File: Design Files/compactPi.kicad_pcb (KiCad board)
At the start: 6 copper layers, 47 x 105 mm, 130 parts, among them J1 1053101208, J10 Conn_01x06_MountingPin, J11 Conn_01x04_MountingPin, J12 Conn_01x02_MountingPin, J13 Conn_01x02_MountingPin, J14 Micro_SD_Card_Det, J15 USB_C_Receptacle_USB2.0, J16 Conn_01x06_MountingPin, J17 Conn_01x06_MountingPin, J18 Conn_01x06_MountingPin, J19 Conn_01x06_MountingPin, J2 HDMI_A_1.4, J3 Conn_01x04_MountingPin, J4 Conn_01x06_MountingPin, J5 Conn_01x04_MountingPin, J6 Conn_01x04_MountingPin, J7 Conn_01x04_MountingPin, J8 Conn_01x04_MountingPin, J9 Conn_01x04_MountingPin, U1 RT9742GGJ5, U13 TLVM13630RDHR, U14 TLVM13630RDHR, U15 AK09918C, U17 RT9742SNGV, U18 PCA9685PW, U19 ICM-20602, U2 AT24CS64-MAHM, U20 MMC5983MA, U21 MCP25625x-x-ML, U22 WE-TVS-82400102, U23 WE-TVS-82400102, U25 BMP390, U4 LM74700QDBVRQ1, U5 CSD18511Q5A, U6 CSD18511Q5A, U7 LM74700QDBVRQ1, U8 CSD18511Q5A, U9 LM74700QDBVRQ1, Y1 Crystal_GND24_Small

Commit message: Added additional ground vias to ethernet nets
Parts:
- moved G*** 4.64 mm to (144.9, 65.3), turned to -90 degrees
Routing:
- net GND: vias 33 -> 41
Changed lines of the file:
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@@
 	(footprint "LOGO"
 		(layer "B.Cu")
-		(at 140.3 64.7 90)
+		(at 144.9 65.3 -90)
 		(property "Reference" "G***"
 			(at 0 0 90)
@@
 				(xy 0.74915 -1.619005) (xy 0.748603 -1.596191) (xy 0.748328 -1.568735) (xy 0.748269 -1.53599) (xy 0.748372 -1.497308)
 				(xy 0.748548 -1.458993) (xy 0.749473 -1.274104) (xy 0.801897 -1.273118) (xy 0.854321 -1.272131)
+			)
+			(stroke
+				(width 0)
+				(type solid)
+			)
+			(fill yes)
+			(layer "B.SilkS")
+		)
+		(fp_poly
+			(pts
+				(xy -0.695313 -1.272295) (xy -0.662953 -1.282153) (xy -0.633599 -1.297835) (xy -0.607944 -1.318779)
+				(xy -0.58668 -1.344421) (xy -0.570498 -1.374199) (xy -0.560211 -1.406976) (xy -0.558999 -1.414101)
+				(xy -0.557981 -1.423469) (xy -0.557141 -1.435672) (xy -0.556466 -1.451302) (xy -0.555941 -1.470949)
+				(xy -0.55555 -1.495207) (xy -0.555279 -1.524666) (xy -0.555112 -1.559919) (xy -0.555036 -1.601556)
+				(xy -0.555029 -1.614044) (xy -0.554967 -1.796951) (xy -0.608501 -1.796951) (xy -0.662035 -1.796951)
+				(xy -0.662106 -1.644379) (xy -0.662204 -1.611007) (xy -0.662456 -1.578981) (xy -0.662843 -1.5492)
+				(xy -0.663347 -1.522559) (xy -0.663949 -1.499954) (xy -0.664632 -1.482283) (xy -0.665376 -1.470441)
+				(xy -0.665733 -1.467201) (xy -0.672772 -1.438931) (xy -0.684784 -1.415502) (xy -0.701378 -1.397241)
+				(xy -0.722161 -1.384474) (xy -0.74674 -1.377526) (xy -0.774685 -1.376721) (xy -0.800997 -1.382033)
+				(xy -0.823447 -1.393306) (xy -0.841754 -1.410327) (xy -0.855637 -1.432884) (xy -0.858828 -1.440518)
+				(xy -0.860373 -1.445006) (xy -0.861658 -1.450061) (xy -0.862708 -1.456344) (xy -0.863547 -1.464516)
+				(xy -0.864198 -1.47524) (xy -0.864683 -1.489175) (xy -0.865028 -1.506984) (xy -0.865255 -1.529327)
+				(xy -0.865387 -1.556866) (xy -0.865449 -1.590262) (xy -0.865463 -1.627465) (xy -0.865463 -1.796951)
+				(xy -0.920805 -1.796951) (xy -0.976146 -1.796951) (xy -0.975231 -1.535527) (xy -0.974315 -1.274104)
+				(xy -0.920782 -1.274104) (xy -0.867248 -1.274104) (xy -0.8662 -1.299961) (xy -0.865151 -1.325818)
+				(xy -0.850735 -1.311966) (xy -0.825406 -1.292467) (xy -0.796048 -1.278801) (xy -0.762603 -1.270947)
+				(xy -0.729987 -1.268826)
 			)
 			(stroke
@@
 				(xy -0.833788 -2.13504) (xy -0.807966 -2.115448) (xy -0.780185 -2.101943) (xy -0.749383 -2.094141)
 				(xy -0.7145 -2.091658)
-			)
-			(stroke
-				(width 0)
-				(type solid)
-			)
-			(fill yes)
-			(layer "B.SilkS")
-		)
-		(fp_poly
-			(pts
-				(xy -0.695313 -1.272295) (xy -0.662953 -1.282153) (xy -0.633599 -1.297835) (xy -0.607944 -1.318779)
-				(xy -0.58668 -1.344421) (xy -0.570498 -1.374199) (xy -0.560211 -1.406976) (xy -0.558999 -1.414101)
-				(xy -0.557981 -1.423469) (xy -0.557141 -1.435672) (xy -0.556466 -1.451302) (xy -0.555941 -1.470949)
-				(xy -0.55555 -1.495207) (xy -0.555279 -1.524666) (xy -0.555112 -1.559919) (xy -0.555036 -1.601556)
-				(xy -0.555029 -1.614044) (xy -0.554967 -1.796951) (xy -0.608501 -1.796951) (xy -0.662035 -1.796951)
-				(xy -0.662106 -1.644379) (xy -0.662204 -1.611007) (xy -0.662456 -1.578981) (xy -0.662843 -1.5492)
-				(xy -0.663347 -1.522559) (xy -0.663949 -1.499954) (xy -0.664632 -1.482283) (xy -0.665376 -1.470441)
-				(xy -0.665733 -1.467201) (xy -0.672772 -1.438931) (xy -0.684784 -1.415502) (xy -0.701378 -1.397241)
-				(xy -0.722161 -1.384474) (xy -0.74674 -1.377526) (xy -0.774685 -1.376721) (xy -0.800997 -1.382033)
-				(xy -0.823447 -1.393306) (xy -0.841754 -1.410327) (xy -0.855637 -1.432884) (xy -0.858828 -1.440518)
-				(xy -0.860373 -1.445006) (xy -0.861658 -1.450061) (xy -0.862708 -1.456344) (xy -0.863547 -1.464516)
-				(xy -0.864198 -1.47524) (xy -0.864683 -1.489175) (xy -0.865028 -1.506984) (xy -0.865255 -1.529327)
-				(xy -0.865387 -1.556866) (xy -0.865449 -1.590262) (xy -0.865463 -1.627465) (xy -0.865463 -1.796951)
-				(xy -0.920805 -1.796951) (xy -0.976146 -1.796951) (xy -0.975231 -1.535527) (xy -0.974315 -1.274104)
-				(xy -0.920782 -1.274104) (xy -0.867248 -1.274104) (xy -0.8662 -1.299961) (xy -0.865151 -1.325818)
-				(xy -0.850735 -1.311966) (xy -0.825406 -1.292467) (xy -0.796048 -1.278801) (xy -0.762603 -1.270947)
-				(xy -0.729987 -1.268826)
 			)
 			(stroke
@@
 	)
 	(gr_text "Copyright © 2026 Logan Fagg, Licensed under CERN-OHL-S v2"
-		(at 146.5 119.3 270)
+		(at 147.3 69.3 90)
 		(layer "B.SilkS")
 		(effects
@@
 	)
 	(via
+		(at 136.9 127.7)
+		(size 0.45)
+		(drill 0.2)
+		(layers "F.Cu" "B.Cu")
+		(free yes)
+		(net 1)
+	)
+	(via
 		(at 142 89.7)
 		(size 0.5)
@@
 	)
 	(via
+		(at 130.3 115.1)
+		(size 0.45)
+		(drill 0.2)
+		(layers "F.Cu" "B.Cu")
+		(free yes)
+		(net 1)
+	)
+	(via
 		(at 108 95.7)
 		(size 0.5)
@@
 	)
 	(via
+		(at 138.1 129.9)
+		(size 0.45)
+		(drill 0.2)
+		(layers "F.Cu" "B.Cu")
+		(free yes)
+		(net 1)
+	)
+	(via
+		(at 140.9 131.3)
+		(size 0.45)
+		(drill 0.2)
+		(layers "F.Cu" "B.Cu")
+		(free yes)
+		(net 1)
+	)
+	(via
 		(at 142 85.2)
 		(size 0.5)
@@
 	)
 	(via
+		(at 127.9 115.1)
+		(size 0.45)
+		(drill 0.2)
+		(layers "F.Cu" "B.Cu")
+		(free yes)
+		(net 1)
+	)
+	(via
 		(at 142 86.7)
 		(size 0.5)
@@
 		(size 0.5)
 		(drill 0.3)
+		(layers "F.Cu" "B.Cu")
+		(free yes)
+		(net 1)
+	)
+	(via
+		(at 121.5 114.9)
+		(size 0.45)
+		(drill 0.2)
+		(layers "F.Cu" "B.Cu")
+		(free yes)
+		(net 1)
+	)
+	(via
+		(at 139.1 125.9)
+		(size 0.45)
+		(drill 0.2)
 		(layers "F.Cu" "B.Cu")
 		(free yes)
@@
 		(layers "F.Cu" "B.Cu")
 		(free yes)
+		(net 1)
+	)
+	(via
+		(at 124.1 114.9)
+		(size 0.45)
+		(drill 0.2)
+		(layers "F.Cu" "B.Cu")
+		(free yes)

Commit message: Added stackup
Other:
- board text added: "0"
- board text added: "0 mm"
- board text added: "0.01 mm"
- board text added: "0.02"
- board text added: "0.035 mm"
- board text added: "0.15 mm"
- board text added: "0.23 mm"
- board text added: "0.38 mm"
- board text added: "1"
- board text added: "3.3"
- board text added: "4.5"
- board text added: "6 layer/1.6mm Stackup Info Source: https://support.macrofab.com/s/article/pcb-layer-stackups"
- board text added: "B.Cu"
- board text added: "B.Mask"
- board text added: "B.Paste"
- board text added: "B.Silkscreen"
- board text added: "Bottom Silk Screen"
- board text added: "Bottom Solder Mask"
- board text added: "Bottom Solder Paste"
- board text added: "Color"
- board text added: "Dielectric 1"
- board text added: "Dielectric 2"
- board text added: "Dielectric 3"
- board text added: "Dielectric 4"
- board text added: "Dielectric 5"
- board text added: "Epsilon R"
- board text added: "F.Cu"
- board text added: "F.Mask"
- board text added: "F.Paste"
- board text added: "F.Silkscreen"
- board text added: "FR4"
- board text added: "In1.Cu"
- board text added: "In2.Cu"
- board text added: "In3.Cu"
- board text added: "In4.Cu"
- board text added: "Layer Name"
- board text added: "Loss Tangent"
- board text added: "Material"
- board text added: "Not specified"
- board text added: "Red"
- board text added: "Thickness (mm)"
- board text added: "Top Silk Screen"
- board text added: "Top Solder Mask"
- board text added: "Top Solder Paste"
- board text added: "Type"
- board text added: "copper"
- board text added: "core"
- board text added: "prepreg"

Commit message: updated skews
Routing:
- net /CM5_HighSpeed/HDMI0_D1_N: track 58.6 -> 63.5 mm
- net /CM5_HighSpeed/HDMI0_CK_N: track 58.5 -> 59.4 mm

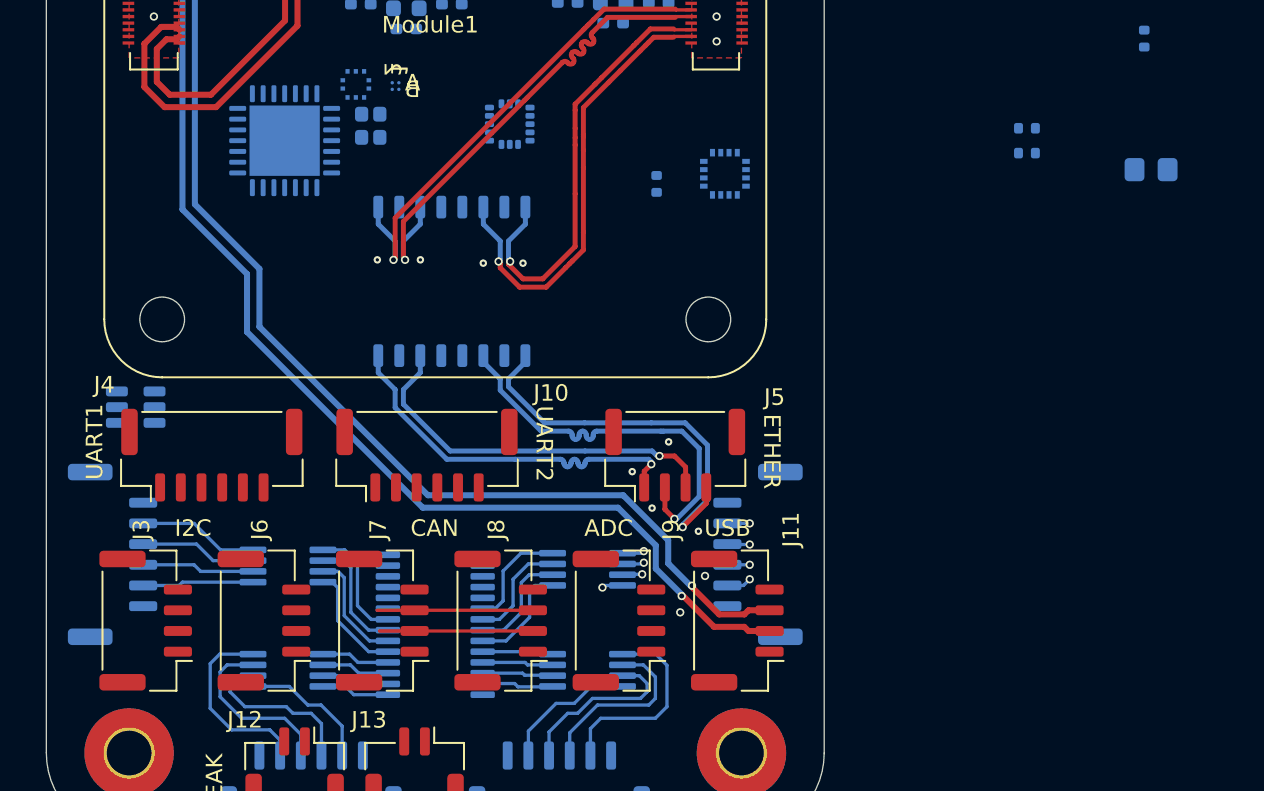
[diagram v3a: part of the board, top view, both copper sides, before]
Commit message: Fixed power & GPIO nets
Added PWM I2C Bus
Replaced global power labels on the sensor page with hierarchical pins & page labels
Cleaned up CM5 GPIO block sheet
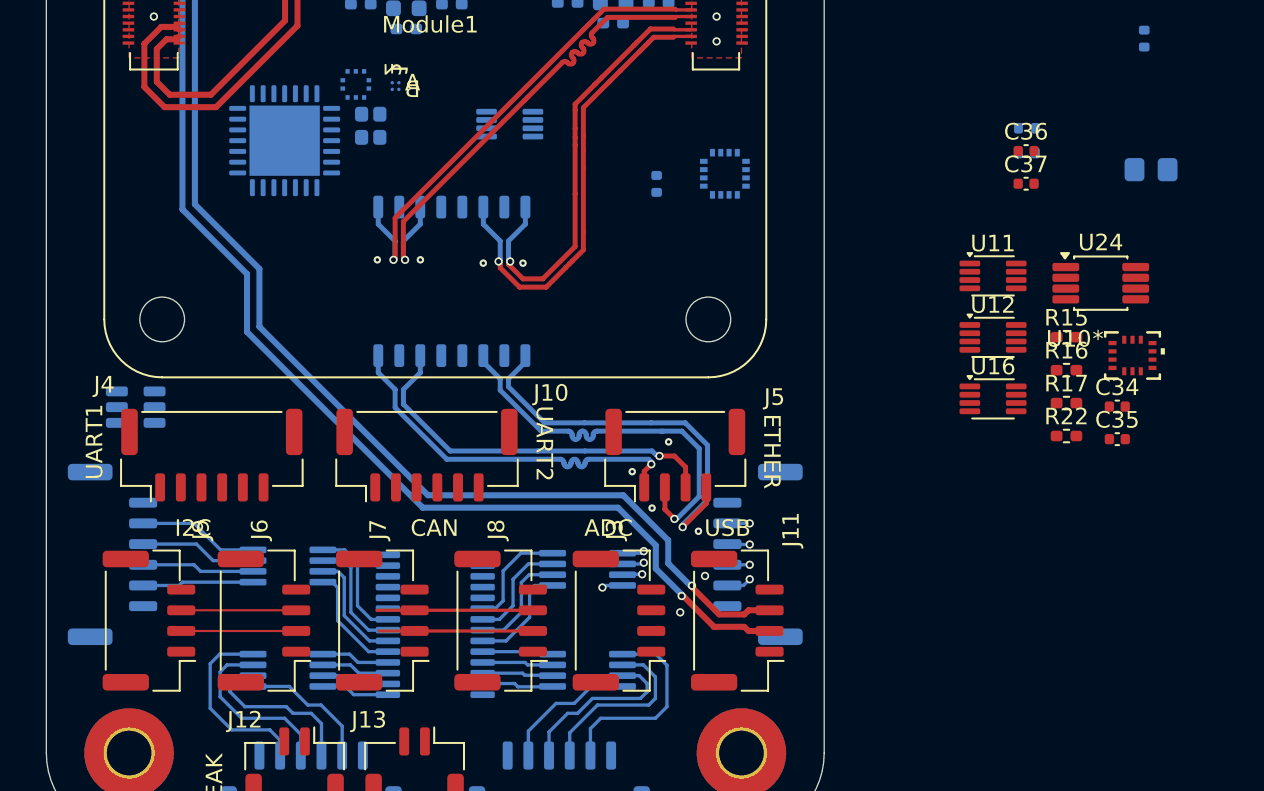
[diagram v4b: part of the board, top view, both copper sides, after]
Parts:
- added C34: 100nF, Capacitor_SMD:C_0402_1005Metric, F.Cu at (166.2, 123.8)
- added C35: 100nF, Capacitor_SMD:C_0402_1005Metric, F.Cu at (166.2, 125.7)
- added C36: 100nF, Capacitor_SMD:C_0402_1005Metric, F.Cu at (160.7, 108.3)
- added C37: 100nF, Capacitor_SMD:C_0402_1005Metric, F.Cu at (160.7, 110.3)
- added R15: 10k, Resistor_SMD:R_0402_1005Metric_Pad0.72x0.64mm_HandSolder, F.Cu at (163.1, 119.6)
- added R16: 10k, Resistor_SMD:R_0402_1005Metric_Pad0.72x0.64mm_HandSolder, F.Cu at (163.1, 121.6)
- added R17: 10k, Resistor_SMD:R_0402_1005Metric_Pad0.72x0.64mm_HandSolder, F.Cu at (163.1, 123.6)
- added R22: 10k, Resistor_SMD:R_0402_1005Metric_Pad0.72x0.64mm_HandSolder, F.Cu at (163.1, 125.5)
- added U10: BMI270, SiGe_Lib:BMI270_BOS, F.Cu at (167.1, 120.7)
- added U11: 74LVC2T45DC, Package_SO:VSSOP-8_2.3x2mm_P0.5mm, F.Cu at (158.7, 115.9)
- added U12: 74LVC2T45DC, Package_SO:VSSOP-8_2.3x2mm_P0.5mm, F.Cu at (158.7, 119.6)
- added U16: 74LVC2T45DC, Package_SO:VSSOP-8_2.3x2mm_P0.5mm, F.Cu at (158.7, 123.3)
- added U24: TCA9517ADGK, Package_SO:VSSOP-8_3x3mm_P0.65mm, F.Cu at (165.2, 116.3)
- C52, C53: value C_Small_US -> 22pF
- U19: value ICM-20602 -> 74LVC2T45DC; footprint Package_LGA:LGA-16_3x3mm_P0.5mm_LayoutBorder3x5y -> Package_SO:VSSOP-8_2.3x2mm_P0.5mm
- moved J3 28.6 mm to (136.1, 136.7)
- moved J9 28.4 mm to (107.7, 136.7)
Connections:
- net /Autopilot IO/PWM_01_PR renamed /PWM IO/PWM_01_PR
- net /Autopilot IO/PWM_02_PR renamed /PWM IO/PWM_02_PR
- net /Autopilot IO/PWM_03_PR renamed /PWM IO/PWM_03_PR
- net /Autopilot IO/PWM_04_PR renamed /PWM IO/PWM_04_PR
- net /Autopilot IO/PWM_05_PR renamed /PWM IO/PWM_05_PR
- net /Autopilot IO/PWM_06_PR renamed /PWM IO/PWM_06_PR
- net /Autopilot IO/PWM_07_PR renamed /PWM IO/PWM_07_PR
- net /Autopilot IO/PWM_08_PR renamed /PWM IO/PWM_08_PR
- net /Autopilot IO/PWM_09_PR renamed /PWM IO/PWM_09_PR
- net /Autopilot IO/PWM_10_PR renamed /PWM IO/PWM_10_PR
- net /Autopilot IO/PWM_11_PR renamed /PWM IO/PWM_11_PR
- net /Autopilot IO/PWM_12_PR renamed /PWM IO/PWM_12_PR
- net /Autopilot IO/PWM_13_PR renamed /PWM IO/PWM_13_PR
- net /Autopilot IO/PWM_14_PR renamed /PWM IO/PWM_14_PR
- net /Autopilot IO/PWM_15_PR renamed /PWM IO/PWM_15_PR
- net /Autopilot IO/PWM_PR_00 renamed /PWM IO/PWM_PR_00
- net /CM5_GPIO ( Ethernet, GPIO, SDCARD)/EEPROM_nWP renamed /CM5 GPIO Ethernet SDIO/EEPROM_nWP
- net /CM5_GPIO ( Ethernet, GPIO, SDCARD)/ETH_LEDG renamed /CM5 GPIO Ethernet SDIO/ETH_LEDG
- net /CM5_GPIO ( Ethernet, GPIO, SDCARD)/ETH_LEDY renamed /CM5 GPIO Ethernet SDIO/ETH_LEDY
- net /CM5_GPIO ( Ethernet, GPIO, SDCARD)/GPIO12 renamed /CM5 GPIO Ethernet SDIO/GPIO12
- net /CM5_GPIO ( Ethernet, GPIO, SDCARD)/GPIO13 renamed /CM5 GPIO Ethernet SDIO/GPIO13
- net /CM5_GPIO ( Ethernet, GPIO, SDCARD)/GPIO14 renamed /CM5 GPIO Ethernet SDIO/GPIO14
- net /CM5_GPIO ( Ethernet, GPIO, SDCARD)/GPIO15 renamed /CM5 GPIO Ethernet SDIO/GPIO15
- net /CM5_GPIO ( Ethernet, GPIO, SDCARD)/GPIO16 renamed /CM5 GPIO Ethernet SDIO/GPIO16
- net /CM5_GPIO ( Ethernet, GPIO, SDCARD)/GPIO17 renamed /SPI_CAN_CE1
- net /CM5_GPIO ( Ethernet, GPIO, SDCARD)/GPIO22 renamed /CM5 GPIO Ethernet SDIO/GPIO22
- net /CM5_GPIO ( Ethernet, GPIO, SDCARD)/GPIO25 renamed /CM5 GPIO Ethernet SDIO/GPIO25
- net /CM5_GPIO ( Ethernet, GPIO, SDCARD)/GPIO27 renamed /CM5 GPIO Ethernet SDIO/GPIO27
- net /CM5_GPIO ( Ethernet, GPIO, SDCARD)/GPIO4 renamed /CM5 GPIO Ethernet SDIO/GPIO4
- net /CM5_GPIO ( Ethernet, GPIO, SDCARD)/GPIO5 renamed /CM5 GPIO Ethernet SDIO/GPIO5
- net /CM5_GPIO ( Ethernet, GPIO, SDCARD)/GPIO_VREF renamed /CM5 GPIO Ethernet SDIO/GPIO_VREF
- net /CM5_GPIO ( Ethernet, GPIO, SDCARD)/ID_SC renamed /CM5 GPIO Ethernet SDIO/ID_SC
- net /CM5_GPIO ( Ethernet, GPIO, SDCARD)/ID_SD renamed /CM5 GPIO Ethernet SDIO/ID_SD
- net /CM5_GPIO ( Ethernet, GPIO, SDCARD)/PMIC_ENABLE renamed /CM5 GPIO Ethernet SDIO/PMIC_ENABLE
- net /CM5_GPIO ( Ethernet, GPIO, SDCARD)/PWM renamed /CM5 GPIO Ethernet SDIO/PWM
- net /CM5_GPIO ( Ethernet, GPIO, SDCARD)/PWR_BUT renamed /CM5 GPIO Ethernet SDIO/PWR_BUT
- net /CM5_GPIO ( Ethernet, GPIO, SDCARD)/SD_CLK renamed /CM5 GPIO Ethernet SDIO/SD_CLK
- net /CM5_GPIO ( Ethernet, GPIO, SDCARD)/SD_CMD renamed /CM5 GPIO Ethernet SDIO/SD_CMD
- net /CM5_GPIO ( Ethernet, GPIO, SDCARD)/SD_DAT0 renamed /CM5 GPIO Ethernet SDIO/SD_DAT0
- net /CM5_GPIO ( Ethernet, GPIO, SDCARD)/SD_DAT1 renamed /CM5 GPIO Ethernet SDIO/SD_DAT1
- net /CM5_GPIO ( Ethernet, GPIO, SDCARD)/SD_DAT2 renamed /CM5 GPIO Ethernet SDIO/SD_DAT2
- net /CM5_GPIO ( Ethernet, GPIO, SDCARD)/SD_DAT3 renamed /CM5 GPIO Ethernet SDIO/SD_DAT3
- net /CM5_GPIO ( Ethernet, GPIO, SDCARD)/SD_PWR renamed /CM5 GPIO Ethernet SDIO/SD_PWR
- net /CM5_GPIO ( Ethernet, GPIO, SDCARD)/SD_PWR_ON renamed /CM5 GPIO Ethernet SDIO/SD_PWR_ON
- net /CM5_GPIO ( Ethernet, GPIO, SDCARD)/SYNC_OUT renamed /CM5 GPIO Ethernet SDIO/SYNC_OUT
- net /CM5_GPIO ( Ethernet, GPIO, SDCARD)/TACHO renamed /CM5 GPIO Ethernet SDIO/TACHO
- net /CM5_GPIO ( Ethernet, GPIO, SDCARD)/TRD0_N renamed /CM5 GPIO Ethernet SDIO/TRD0_N
- net /CM5_GPIO ( Ethernet, GPIO, SDCARD)/TRD0_P renamed /CM5 GPIO Ethernet SDIO/TRD0_P
- net /CM5_GPIO ( Ethernet, GPIO, SDCARD)/TRD0_TX_N renamed /CM5 GPIO Ethernet SDIO/TRD0_TX_N
- net /CM5_GPIO ( Ethernet, GPIO, SDCARD)/TRD0_TX_P renamed /CM5 GPIO Ethernet SDIO/TRD0_TX_P
- net /CM5_GPIO ( Ethernet, GPIO, SDCARD)/TRD1_N renamed /CM5 GPIO Ethernet SDIO/TRD1_N
- net /CM5_GPIO ( Ethernet, GPIO, SDCARD)/TRD1_P renamed /CM5 GPIO Ethernet SDIO/TRD1_P
- net /CM5_GPIO ( Ethernet, GPIO, SDCARD)/TRD1_RX_N renamed /CM5 GPIO Ethernet SDIO/TRD1_RX_N
- net /CM5_GPIO ( Ethernet, GPIO, SDCARD)/TRD1_RX_P renamed /CM5 GPIO Ethernet SDIO/TRD1_RX_P
- net /CM5_GPIO ( Ethernet, GPIO, SDCARD)/VBAT renamed /CM5 GPIO Ethernet SDIO/VBAT
- net /CM5_GPIO ( Ethernet, GPIO, SDCARD)/nPWR_LED renamed /CM5 GPIO Ethernet SDIO/nPWR_LED
- net /CM5_HighSpeed/DPHY1_D3_N renamed /CM5 USB HDMI/DPHY1_D3_N
- net /CM5_HighSpeed/DPHY1_D3_P renamed /CM5 USB HDMI/DPHY1_D3_P
- net /CM5_HighSpeed/HDMI0_CEC renamed /CM5 USB HDMI/HDMI0_CEC
- net /CM5_HighSpeed/HDMI0_CK_N renamed /CM5 USB HDMI/HDMI0_CK_N
- net /CM5_HighSpeed/HDMI0_CK_P renamed /CM5 USB HDMI/HDMI0_CK_P
- net /CM5_HighSpeed/HDMI0_D0_N renamed /CM5 USB HDMI/HDMI0_D0_N
- net /CM5_HighSpeed/HDMI0_D0_P renamed /CM5 USB HDMI/HDMI0_D0_P
- net /CM5_HighSpeed/HDMI0_D1_N renamed /CM5 USB HDMI/HDMI0_D1_N
- net /CM5_HighSpeed/HDMI0_D1_P renamed /CM5 USB HDMI/HDMI0_D1_P
- net /CM5_HighSpeed/HDMI0_D2_N renamed /CM5 USB HDMI/HDMI0_D2_N
- net /CM5_HighSpeed/HDMI0_D2_P renamed /CM5 USB HDMI/HDMI0_D2_P
- net /CM5_HighSpeed/HDMI0_HOTPLUG renamed /CM5 USB HDMI/HDMI0_HOTPLUG
- net /CM5_HighSpeed/HDMI0_SCL renamed /CM5 USB HDMI/HDMI0_SCL
- net /CM5_HighSpeed/HDMI0_SDA renamed /CM5 USB HDMI/HDMI0_SDA
- net /CM5_HighSpeed/HDMI_5v renamed /CM5 USB HDMI/HDMI_5v
- net /CM5_HighSpeed/PCIE_CLK_N renamed /CM5 USB HDMI/PCIE_CLK_N
- net /CM5_HighSpeed/PCIE_CLK_P renamed /CM5 USB HDMI/PCIE_CLK_P
- net /CM5_HighSpeed/PCIE_PWR_EN renamed /CM5 USB HDMI/PCIE_PWR_EN
- net /CM5_HighSpeed/PCIE_RX_N renamed /CM5 USB HDMI/PCIE_RX_N
- net /CM5_HighSpeed/PCIE_RX_P renamed /CM5 USB HDMI/PCIE_RX_P
- net /CM5_HighSpeed/PCIE_TX_N renamed /CM5 USB HDMI/PCIE_TX_N
- net /CM5_HighSpeed/PCIE_TX_P renamed /CM5 USB HDMI/PCIE_TX_P
- net /CM5_HighSpeed/PCIE_nCLKREQ renamed /CM5 USB HDMI/PCIE_nCLKREQ
- net /CM5_HighSpeed/PCIE_nRST renamed /CM5 USB HDMI/PCIE_nRST
- net /CM5_HighSpeed/PCIE_nWAKE renamed /CM5 USB HDMI/PCIE_nWAKE
- net /CM5_HighSpeed/USB3-0-RX_N renamed /CM5 USB HDMI/USB3-0-RX_N
- net /CM5_HighSpeed/USB3-0-RX_P renamed /CM5 USB HDMI/USB3-0-RX_P
- net /CM5_HighSpeed/USB3-0-TX_N renamed /CM5 USB HDMI/USB3-0-TX_N
- net /CM5_HighSpeed/USB3-0-TX_P renamed /CM5 USB HDMI/USB3-0-TX_P
- net /CM5_HighSpeed/USB3-1-D_N renamed /CM5 USB HDMI/USB3-1-D_N
- net /CM5_HighSpeed/USB3-1-D_P renamed /CM5 USB HDMI/USB3-1-D_P
- net /CM5_HighSpeed/USB3-1-RX_N renamed /CM5 USB HDMI/USB3-1-RX_N
- net /CM5_HighSpeed/USB3-1-RX_P renamed /CM5 USB HDMI/USB3-1-RX_P
- net /CM5_HighSpeed/USB3-1-TX_N renamed /CM5 USB HDMI/USB3-1-TX_N
- net /CM5_HighSpeed/USB3-1-TX_P renamed /CM5 USB HDMI/USB3-1-TX_P
- net /CM5_HighSpeed/USBOTG_ID renamed /CM5 USB HDMI/USBOTG_ID
- net Net-(J7-Pin_2) renamed /Autopilot Interfaces/CAN_H
- net Net-(J7-Pin_3) renamed /Autopilot Interfaces/CAN_L
- C41 pad 1: /VBUS -> /5V0_PERIPHERAL
- C55 pad 1: Net-(U15-VDD) -> /1V8
- C57 pad 1: unconnected-(C57-Pad1) -> /1V8
- C57 pad 2: unconnected-(C57-Pad2) -> GND
- C58 pad 1: unconnected-(C58-Pad1) -> /1V8
- C58 pad 2: unconnected-(C58-Pad2) -> GND
- C59 pad 1: unconnected-(C59-Pad1) -> /1V8
- C59 pad 2: unconnected-(C59-Pad2) -> GND
- C60 pad 1: unconnected-(C60-Pad1) -> /1V8
- C60 pad 2: unconnected-(C60-Pad2) -> GND
- C61 pad 1: unconnected-(C61-Pad1) -> /3V3
- C61 pad 2: unconnected-(C61-Pad2) -> GND
- C62 pad 1: unconnected-(C62-Pad1) -> Net-(U20-VDDIO)
- C62 pad 2: unconnected-(C62-Pad2) -> GND
- C63 pad 1: unconnected-(C63-Pad1) -> Net-(U20-CAP)
- C63 pad 2: unconnected-(C63-Pad2) -> GND
- D3 pad 2: /+3.3v -> /3V3
- D4 pad 2: /+3.3v -> /3V3
- J10 pad 1: unconnected-(J10-Pin_1-Pad1) -> /5V0_PERIPHERAL
- J10 pad 2: unconnected-(J10-Pin_2-Pad2) -> /Autopilot Interfaces/UART2_RX_In
- J10 pad 3: unconnected-(J10-Pin_3-Pad3) -> /Autopilot Interfaces/UART2_TX_Out
- J10 pad 6: unconnected-(J10-Pin_6-Pad6) -> GND
- J11 pad 1: /VBUS -> /5V0_PERIPHERAL
- J16 pad 1: unconnected-(J16-Pin_1-Pad1) -> /5V0_PERIPHERAL
- J16 pad 6: unconnected-(J16-Pin_6-Pad6) -> GND
- J17 pad 1: unconnected-(J17-Pin_1-Pad1) -> /5V0_PERIPHERAL
- J17 pad 6: unconnected-(J17-Pin_6-Pad6) -> GND
- J18 pad 1: unconnected-(J18-Pin_1-Pad1) -> /5V0_PERIPHERAL
- J18 pad 6: unconnected-(J18-Pin_6-Pad6) -> GND
- J19 pad 1: unconnected-(J19-Pin_1-Pad1) -> /5V0_PERIPHERAL
- J19 pad 6: unconnected-(J19-Pin_6-Pad6) -> GND
- J4 pad 1: unconnected-(J4-Pin_1-Pad1) -> /5V0_PERIPHERAL
- J4 pad 2: unconnected-(J4-Pin_2-Pad2) -> /Autopilot Interfaces/UART1_RX_In
- J4 pad 3: unconnected-(J4-Pin_3-Pad3) -> /Autopilot Interfaces/UART1_TX_Out
- J4 pad 6: unconnected-(J4-Pin_6-Pad6) -> GND
- J6 pad 1: unconnected-(J6-Pin_1-Pad1) -> /5V0_PERIPHERAL
- J6 pad 2: unconnected-(J6-Pin_2-Pad2) -> /I2C_EXT_SCL1
- J6 pad 3: unconnected-(J6-Pin_3-Pad3) -> /I2C_EXT_SDA1
- J6 pad 4: unconnected-(J6-Pin_4-Pad4) -> GND
- J7 pad 1: /CM5_GPIO ( Ethernet, GPIO, SDCARD)/+5V -> /5V0_PERIPHERAL
- J8 pad 1: /CM5_GPIO ( Ethernet, GPIO, SDCARD)/+5V -> /5V0_PERIPHERAL
- J9 pad 1: unconnected-(J9-Pin_1-Pad1) -> /5V0_PERIPHERAL
- J9 pad 2: unconnected-(J9-Pin_2-Pad2) -> /I2C_EXT_SCL1
- J9 pad 3: unconnected-(J9-Pin_3-Pad3) -> /I2C_EXT_SDA1
- J9 pad 4: unconnected-(J9-Pin_4-Pad4) -> GND
- Module1 pad 100: /CM5_GPIO ( Ethernet, GPIO, SDCARD)/CAM_GPIO1 -> unconnected-(Module1A-CAM_GPIO1-Pad100)
- Module1 pad 24: /CM5_GPIO ( Ethernet, GPIO, SDCARD)/GPIO26 -> unconnected-(Module1A-GPIO26-Pad24)
- Module1 pad 25: /CM5_GPIO ( Ethernet, GPIO, SDCARD)/GPIO21 -> /SPI_CAN_SCK
- Module1 pad 26: /CM5_GPIO ( Ethernet, GPIO, SDCARD)/GPIO19 -> /SPI_CAN_COPI
- Module1 pad 27: /CM5_GPIO ( Ethernet, GPIO, SDCARD)/GPIO20 -> /SPI_CAN_CIPO
- Module1 pad 30: /CM5_GPIO ( Ethernet, GPIO, SDCARD)/GPIO6 -> /I2C_PWM_SDA
- Module1 pad 37: /CM5_GPIO ( Ethernet, GPIO, SDCARD)/GPIO7 -> /I2C_PWM_SCL
- Module1 pad 38: /CM5_GPIO ( Ethernet, GPIO, SDCARD)/GPIO11 -> /SPI_INT_SCK
- Module1 pad 39: /CM5_GPIO ( Ethernet, GPIO, SDCARD)/GPIO8 -> /SPI_INT_CE0
- Module1 pad 40: /CM5_GPIO ( Ethernet, GPIO, SDCARD)/GPIO9 -> /SPI_INT_COPI
- Module1 pad 44: /CM5_GPIO ( Ethernet, GPIO, SDCARD)/GPIO10 -> /SPI_INT_CIPO
- Module1 pad 45: /CM5_GPIO ( Ethernet, GPIO, SDCARD)/GPIO24 -> unconnected-(Module1A-GPIO24-Pad45)
- Module1 pad 47: /CM5_GPIO ( Ethernet, GPIO, SDCARD)/GPIO23 -> unconnected-(Module1A-GPIO23-Pad47)
- Module1 pad 49: /CM5_GPIO ( Ethernet, GPIO, SDCARD)/GPIO18 -> /SPI_CAN_CE0
- Module1 pad 56: /CM5_GPIO ( Ethernet, GPIO, SDCARD)/GPIO3 -> /I2C_EXT_SCL1
- Module1 pad 58: /CM5_GPIO ( Ethernet, GPIO, SDCARD)/GPIO2 -> /I2C_EXT_SDA1
- Module1 pad 77: /VBUS -> /5V0_CORE
- Module1 pad 79: /VBUS -> /5V0_CORE
- Module1 pad 80: /CM5_GPIO ( Ethernet, GPIO, SDCARD)/SCL0 -> /I2C_INT_SCL0
- Module1 pad 81: /VBUS -> /5V0_CORE
- Module1 pad 82: /CM5_GPIO ( Ethernet, GPIO, SDCARD)/SDA0 -> /I2C_INT_SDA0
- Module1 pad 83: /VBUS -> /5V0_CORE
- Module1 pad 84: /+3.3v -> /3V3
- Module1 pad 85: /VBUS -> /5V0_CORE
- Module1 pad 86: /+3.3v -> /3V3
- Module1 pad 87: /VBUS -> /5V0_CORE
- Module1 pad 88: /CM5_GPIO ( Ethernet, GPIO, SDCARD)/+1.8v -> /1V8
- Module1 pad 90: /CM5_GPIO ( Ethernet, GPIO, SDCARD)/+1.8v -> /1V8
- Module1 pad 97: /CM5_GPIO ( Ethernet, GPIO, SDCARD)/CAM_GPIO0 -> unconnected-(Module1A-CAM_GPIO0-Pad97)
- R3 pad 1: /+3.3v -> /3V3
- R4 pad 1: /+3.3v -> /3V3
- U1 pad 5: /+3.3v -> /3V3
- U15 pad A2: unconnected-(U15-SCL-PadA2) -> /Autopilot Sensors/I2C_SCL_1V8
- U15 pad B1: Net-(U15-VDD) -> /1V8
- U15 pad B2: unconnected-(U15-SDA-PadB2) -> /Autopilot Sensors/I2C_SDA_1V8
- U17 pad 1: /VBUS -> /5V0_PERIPHERAL
- U18 pad 14: unconnected-(U18-VSS-Pad14) -> GND
- U18 pad 26: unconnected-(U18-SCL-Pad26) -> /I2C_PWM_SCL
- U18 pad 27: unconnected-(U18-SDA-Pad27) -> /I2C_PWM_SDA
- U18 pad 28: unconnected-(U18-VDD-Pad28) -> /3V3
- U19 pad 1: unconnected-(U19-VDDIO-Pad1) -> /3V3
- U19 pad 2: unconnected-(U19-SCL/SPC-Pad2) -> /Autopilot Sensors/INT_IMU1_3V3
- U19 pad 3: unconnected-(U19-SDA/SDI-Pad3) -> /Autopilot Sensors/INT_IMU2_3V3
- U19 pad 4: unconnected-(U19-SAO/SD0-Pad4) -> GND
- U19 pad 5: unconnected-(U19-~{CS}-Pad5) -> GND
- U19 pad 6: unconnected-(U19-INT-Pad6) -> /Autopilot Sensors/INT_IMU2_1V8
- U19 pad 7: unconnected-(U19-RESV-Pad7) -> /Autopilot Sensors/INT_IMU1_1V8
- U19 pad 8: unconnected-(U19-FSYNC-Pad8) -> /1V8
- U20 pad 1: unconnected-(U20-SCL/SPI_SCK-Pad1) -> /I2C_INT_SCL0
- U20 pad 10: unconnected-(U20-CAP-Pad10) -> Net-(U20-CAP)
- U20 pad 11: unconnected-(U20-GND-Pad11) -> GND
- U20 pad 13: unconnected-(U20-VDDIO-Pad13) -> Net-(U20-VDDIO)
- U20 pad 15: unconnected-(U20-INT-Pad15) -> /Autopilot Sensors/INT_MAG_3V3
- U20 pad 16: unconnected-(U20-SDA/SPI_SDI-Pad16) -> /I2C_INT_SDA0
- U20 pad 2: unconnected-(U20-VDD-Pad2) -> /3V3
- U20 pad 9: unconnected-(U20-GND-Pad9) -> GND
- U21 pad 1: unconnected-(U21-~{CS}-Pad1) -> /SPI_CAN_CE0
- U21 pad 10: unconnected-(U21-R_{XD}-Pad10) -> Net-(U21-R_{XD})
- U21 pad 11: /CM5_GPIO ( Ethernet, GPIO, SDCARD)/+5V -> /3V3
- U21 pad 16: unconnected-(U21-T_{XD}-Pad16) -> Net-(U21-T_{XD})
- U21 pad 19: /CM5_GPIO ( Ethernet, GPIO, SDCARD)/+5V -> /5V0_PERIPHERAL
- U21 pad 25: unconnected-(U21-~{INT}-Pad25) -> /Autopilot Interfaces/SPI_CAN_INT_3V3
- U21 pad 26: unconnected-(U21-SCK-Pad26) -> /SPI_CAN_SCK
- U21 pad 27: unconnected-(U21-SI-Pad27) -> /SPI_CAN_COPI
- U21 pad 28: unconnected-(U21-SO-Pad28) -> /SPI_CAN_CIPO
- U21 pad 3: /CM5_GPIO ( Ethernet, GPIO, SDCARD)/+5V -> /5V0_PERIPHERAL
- U21 pad 4: unconnected-(U21-TxCAN-Pad4) -> Net-(U21-T_{XD})
- U21 pad 5: unconnected-(U21-RxCAN-Pad5) -> Net-(U21-R_{XD})
- U25 pad 1: unconnected-(U25-VDDIO-Pad1) -> /1V8
- U25 pad 10: unconnected-(U25-VDD-Pad10) -> /1V8
- U25 pad 2: unconnected-(U25-SCK-Pad2) -> /Autopilot Sensors/SPI_SCK_1V8
- U25 pad 3: unconnected-(U25-VSS-Pad3) -> GND
- U25 pad 4: unconnected-(U25-SDI-Pad4) -> /Autopilot Sensors/SPI_COPI_1V8
- U25 pad 5: unconnected-(U25-SDO-Pad5) -> /Autopilot Sensors/SPI_CIPO_1V8
- U25 pad 6: unconnected-(U25-CSB-Pad6) -> /Autopilot Sensors/CS_PRES_1V8
- U25 pad 7: unconnected-(U25-INT-Pad7) -> /Autopilot Sensors/INT_PRES_1V8
- U25 pad 8: unconnected-(U25-VSS-Pad8) -> GND
- U25 pad 9: unconnected-(U25-VSS-Pad9) -> GND
- U3 pad 28: /CC1 -> /Power/USB_CC1
- U3 pad 29: /CC2 -> /Power/USB_CC2
- U3 pad 34: /5V0_PERIPHERAL -> /Power/5V_PERIPHERAL
- U3 pad 35: /5V0_PERIPHERAL -> /Power/5V_PERIPHERAL
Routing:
- net /I2C_EXT_SDA1: track 0.00 -> 6.95 mm
- net /I2C_EXT_SCL1: track 0.00 -> 6.95 mm
